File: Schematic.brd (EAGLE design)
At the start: 84 x 96 mm, 64 parts

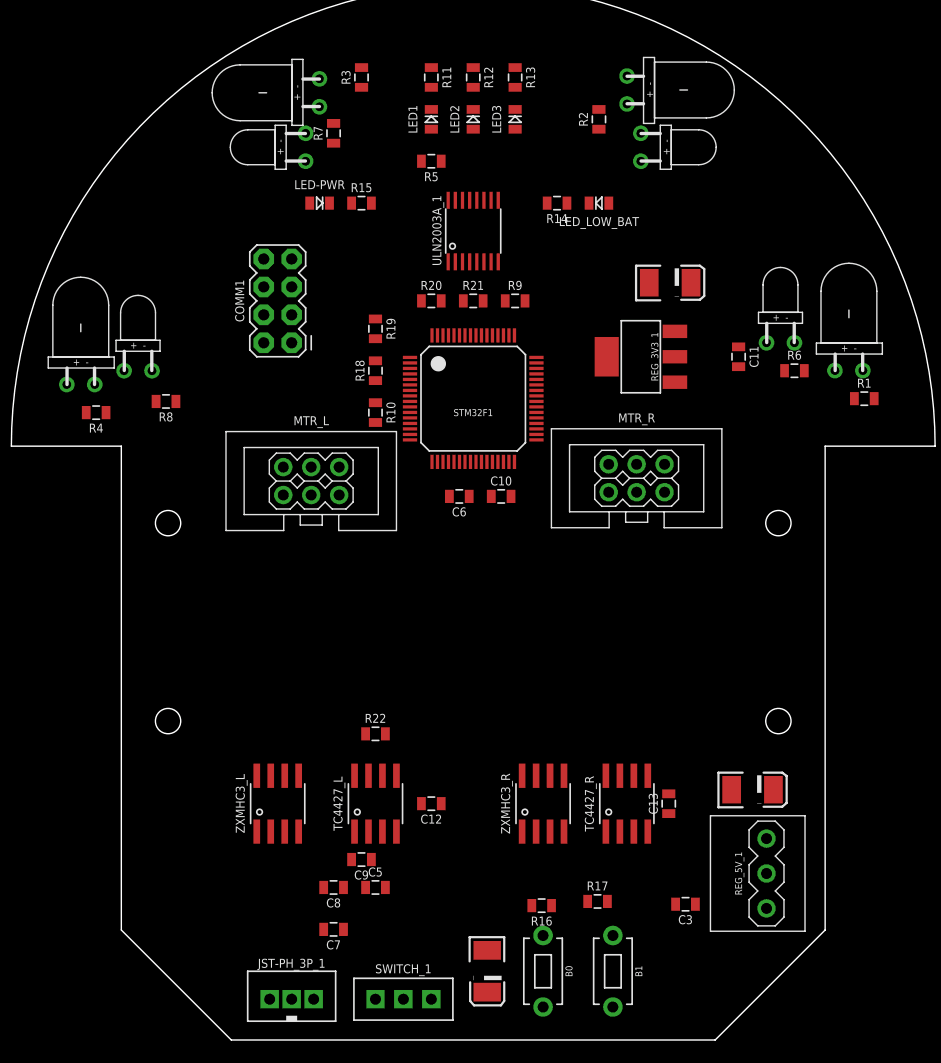
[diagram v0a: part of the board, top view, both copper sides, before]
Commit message: Autoroute only
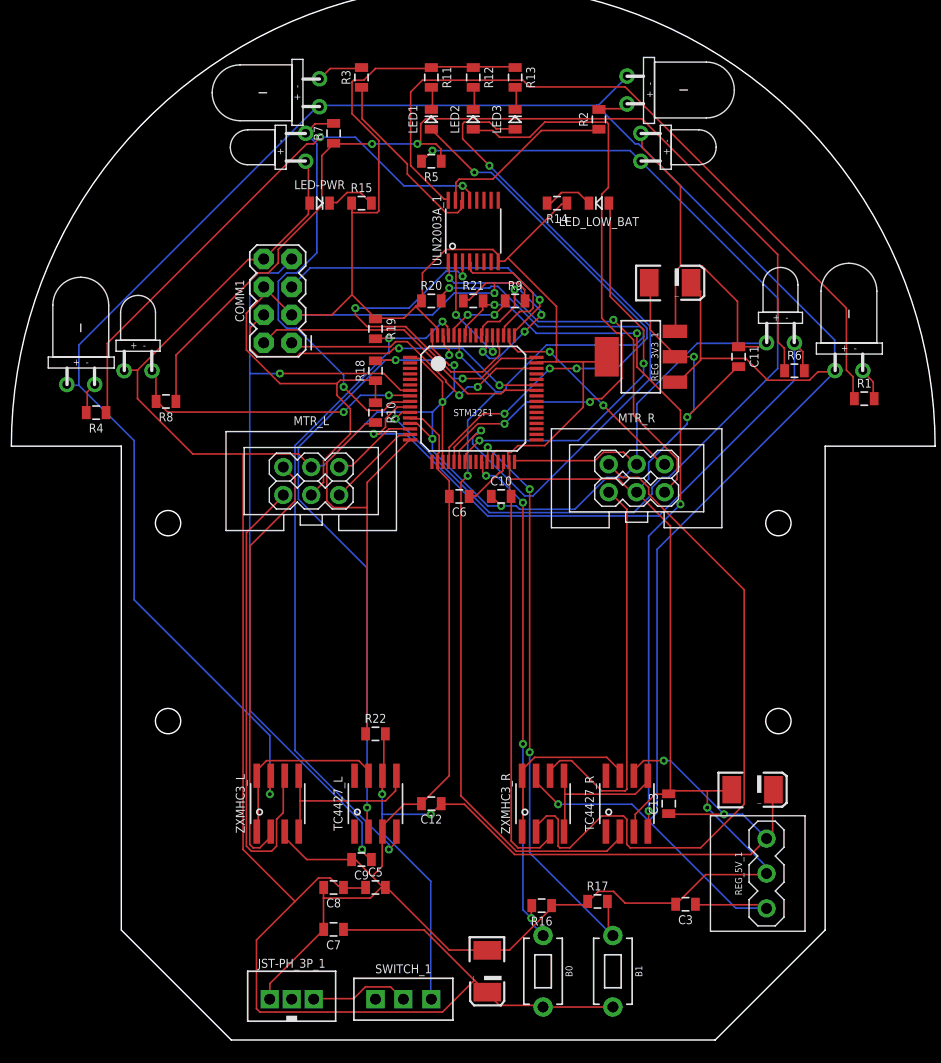
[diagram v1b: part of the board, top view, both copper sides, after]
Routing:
- net GND: track 0.00 -> 425.7 mm, vias 0 -> 4
- net +3V3: track 0.00 -> 295.1 mm, vias 0 -> 5
- net +5V: track 0.00 -> 249.3 mm, vias 0 -> 2
- net RPWM_A: track 0.00 -> 99.3 mm, vias 0 -> 3
- net N$14: track 0.00 -> 91.4 mm, vias 0 -> 2
- net RE_LF: track 0.00 -> 90.4 mm, vias 0 -> 2
- net V+: track 0.00 -> 89.9 mm, vias 0 -> 4
- net NRST: track 0.00 -> 77.1 mm, vias 0 -> 2
- net N$1: track 0.00 -> 68.7 mm
- net RPWM_B: track 0.00 -> 67.5 mm, vias 0 -> 4
- net RMTR+: track 0.00 -> 64.7 mm
- net LPWM_B: track 0.00 -> 63.7 mm, vias 0 -> 3
- net LED3: track 0.00 -> 63.3 mm, vias 0 -> 2
- net LPWM_A: track 0.00 -> 58.7 mm, vias 0 -> 3
- net RE_LD: track 0.00 -> 57.6 mm, vias 0 -> 1
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
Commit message: 013120meeting
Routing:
- net GND: track 425.7 -> 4.02 mm, vias 4 -> 0
- net +3V3: track 295.1 -> 242.1 mm, vias 5 -> 3
- net RPWM_A: track 99.3 -> 57.8 mm, vias 3 -> 2
- net RE_LF: track 90.4 -> 49.1 mm, vias 2 -> 4
- net RMTR+: track 64.7 -> 36.2 mm
- net LED3: track 63.3 -> 36.2 mm
- net LED2: track 56.7 -> 80.9 mm
- net +5V: track 249.3 -> 225.9 mm
- net EM_RD: track 31.0 -> 8.01 mm
- net EM_LD: track 11.1 -> 33.4 mm, vias 2 -> 6
- net N$1: track 68.7 -> 46.5 mm, vias 0 -> 2
- net V+: track 89.9 -> 70.5 mm, vias 4 -> 3
- net LMTR-: track 43.2 -> 25.6 mm
- net LED1: track 51.5 -> 34.1 mm, vias 4 -> 2
- net RE_LD: track 57.6 -> 40.5 mm
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- added copper zone on layer 1, net GND
- added copper zone on layer 16, net GND

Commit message: handroute
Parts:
- removed U$1: (no value), MOUSE_OUTLINE_2WHEEL:MOUSE_OUTLINE_2WHEEL
- added U$2: (no value), MOUSE_OUTLINE_2WHEEL:MOUSE_OUTLINE_2WHEEL
- moved SWITCH_1 116.4 mm to (-44.5, 92.7)
- moved C4 114.6 mm to (-35.6, 94.0), turned to 0 degrees
- moved LED3 113.5 mm to (-73.7, 92.7), turned to 0 degrees
- moved C1 108.8 mm to (-20.3, 94.0)
- moved B1 108.5 mm to (-55.2, 37.5), turned to 0 degrees
- moved LED2 105.9 mm to (-69.8, 92.7), turned to 0 degrees
- moved B0 104.2 mm to (-54.6, 44.5), turned to 0 degrees
- moved LED_LOW_BAT 101.9 mm to (-53.3, 92.7), turned to 0 degrees
- moved LED1 98.3 mm to (-66.0, 92.7), turned to 0 degrees
- moved R17 98.0 mm to (15.2, 104.1)
- moved C3 96.3 mm to (80.0, 104.1), turned to 0 degrees
- moved R16 95.8 mm to (19.1, 104.1), turned to 0 degrees
- moved JST-PH_3P_1 95.6 mm to (-12.7, 92.7)
- moved R1 90.3 mm to (-18.4, 45.1), turned to 180 degrees
- moved EM_1 89.6 mm to (-19.1, 48.3)
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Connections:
- removed net N$14: R5.1, R6.1, R7.1, R8.1
- net GND: now also R5.1, R6.1, R7.1, R8.1
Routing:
- net +3V3: track 242.1 -> 143.8 mm, vias 3 -> 0
- net N$14: track 91.5 -> 0.00 mm, vias 3 -> 0
- net LED2: track 80.9 -> 0.00 mm, vias 2 -> 0
- net NRST: track 71.6 -> 2.72 mm, vias 2 -> 0
- net B1: track 62.0 -> 0.00 mm, vias 2 -> 0
- net RPWM_B: track 60.4 -> 3.54 mm, vias 2 -> 0
- net RPWM_A: track 57.8 -> 3.54 mm, vias 2 -> 0
- net LPWM_B: track 55.6 -> 4.18 mm, vias 4 -> 0
- net LPWM_A: track 54.0 -> 4.18 mm, vias 2 -> 0
- net B0: track 47.6 -> 0.00 mm
- net RE_LF: track 49.1 -> 2.74 mm, vias 4 -> 0
- net RE_LD: track 40.5 -> 2.25 mm, vias 1 -> 0
- net LED3: track 36.2 -> 0.00 mm, vias 2 -> 0
- net RX: track 35.6 -> 0.00 mm, vias 1 -> 0
- net VOLTMETER: track 35.5 -> 0.00 mm, vias 2 -> 0
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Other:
- outline, holes or cut-outs redrawn

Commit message: Routing
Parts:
- moved SWITCH_1 122.9 mm to (22.9, -10.2)
- moved LED3 117.9 mm to (18.4, 19.1)
- moved LED2 112.5 mm to (15.2, 19.1)
- moved JST-PH_3P_1 112.3 mm to (32.4, -10.2)
- moved C1 108.3 mm to (23.5, -5.08)
- moved C2 107.7 mm to (23.5, -0.64)
- moved LED1 107.4 mm to (12.1, 19.1)
- moved R10 96.2 mm to (5.08, 15.2)
- moved R11 92.6 mm to (12.1, 15.2)
- moved LED_LOW_BAT 91.3 mm to (15.2, 32.4), turned to 270 degrees
- moved R12 90.9 mm to (15.2, 15.2)
- moved R13 89.7 mm to (18.4, 15.2)
- moved R22 89.7 mm to (8.26, 15.2)
- moved LED-PWR 89.1 mm to (29.8, 56.5)
- moved C3 82.1 mm to (21.8, 46.2), turned to 180 degrees
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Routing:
- net LPWM_B: track 4.18 -> 63.3 mm
- net LPWM_A: track 4.18 -> 62.5 mm
- net +3V3: track 143.8 -> 187.2 mm
- net VOLTMETER: track 0.00 -> 24.5 mm
- net NRST: track 2.72 -> 27.0 mm, vias 0 -> 1
- net RX: track 0.00 -> 23.0 mm, vias 0 -> 1
- net TX: track 0.00 -> 21.7 mm, vias 0 -> 1
- net SWCLK: track 0.00 -> 19.2 mm, vias 0 -> 1
- net SWDIO: track 0.00 -> 18.6 mm, vias 0 -> 1
- net LED3: track 0.00 -> 18.5 mm
- net LED2: track 0.00 -> 17.5 mm
- net LED1: track 0.00 -> 17.2 mm
- net V+: track 62.8 -> 78.5 mm, vias 0 -> 1
- net B0: track 0.00 -> 14.1 mm
- net N$9: track 0.00 -> 13.9 mm
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
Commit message: Finished routing
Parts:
- moved REG_3V3_1 4.45 mm to (25.4, 56.5)
- moved C4 3.81 mm to (31.8, 55.2)
- moved LED-PWR 3.17 mm to (29.8, 59.7)
- moved R15 3.17 mm to (33.0, 59.7)
- moved C10 2.54 mm to (3.81, 39.4)
- moved C3 0.90 mm to (21.2, 46.9)
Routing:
- net RPWM_A: track 3.54 -> 59.2 mm, vias 0 -> 4
- net RPWM_B: track 3.54 -> 56.5 mm, vias 0 -> 4
- net +3V3: track 187.2 -> 229.3 mm, vias 0 -> 2
- net RE_LF: track 2.74 -> 43.2 mm, vias 0 -> 3
- net RE_RD: track 2.65 -> 42.1 mm, vias 0 -> 2
- net RE_RF: track 2.26 -> 37.7 mm, vias 0 -> 3
- net RE_LD: track 2.25 -> 27.3 mm, vias 0 -> 2
- net SWDIO: track 18.6 -> 22.1 mm
- net RX: track 23.0 -> 25.4 mm
- net TX: track 21.7 -> 23.6 mm
- net +5V: track 250.0 -> 251.7 mm
- net V+: track 78.5 -> 77.0 mm
- net LED3: track 18.5 -> 20.0 mm
- net RMTR-: track 37.4 -> 36.3 mm
- net LPWM_A: track 62.5 -> 61.4 mm
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
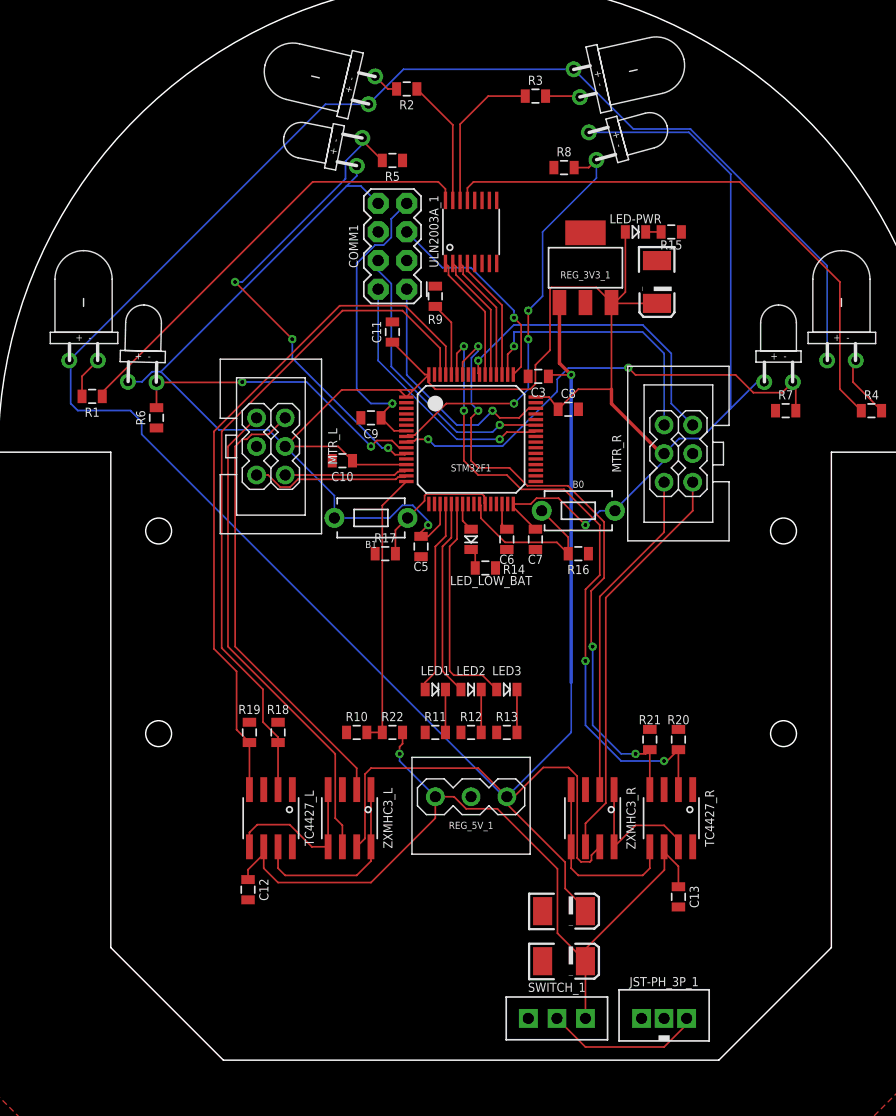
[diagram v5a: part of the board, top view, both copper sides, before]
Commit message: changes trace width
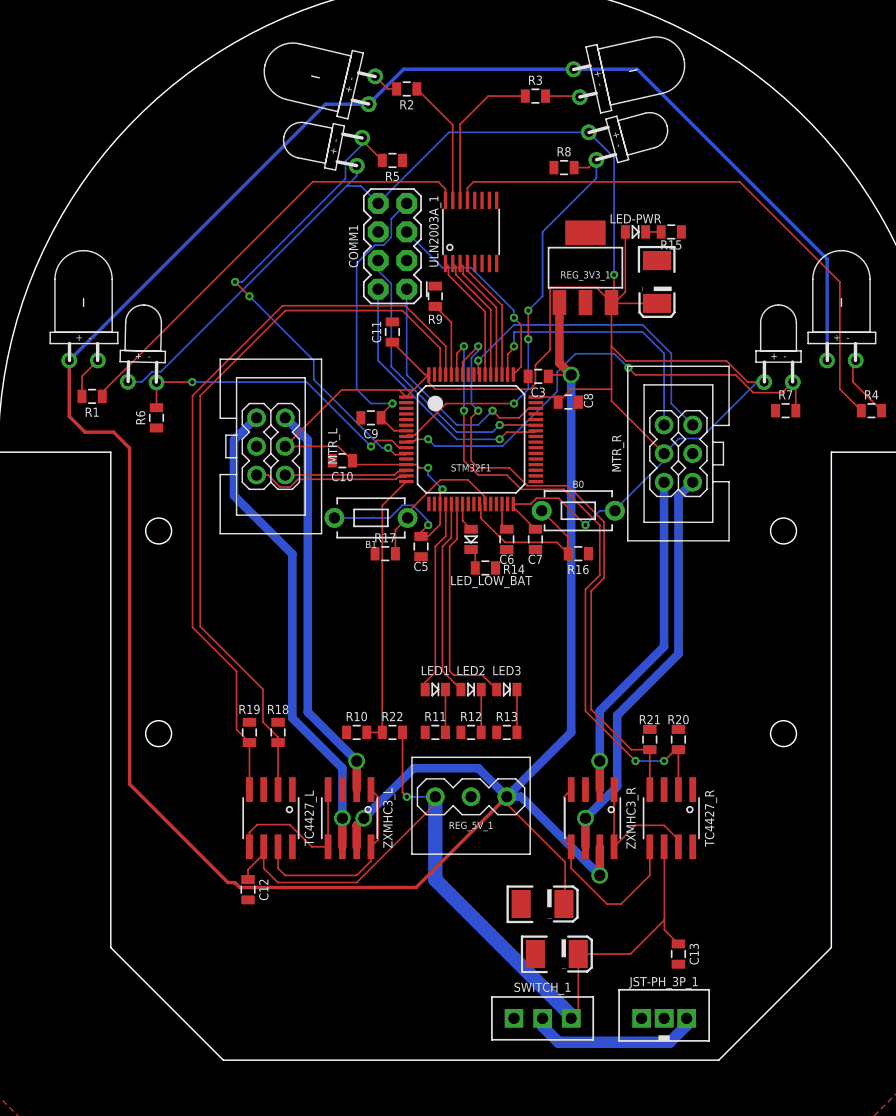
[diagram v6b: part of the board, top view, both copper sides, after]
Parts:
- moved C13 5.08 mm to (33.7, -4.45)
- moved C2 2.01 mm to (21.6, 0.00)
- moved SWITCH_1 1.27 mm to (21.6, -10.2)
- moved C1 0.90 mm to (22.9, -4.45)
- moved C8 0.63 mm to (23.9, 44.6)
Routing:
- net +5V: track 251.7 -> 268.6 mm, vias 1 -> 3
- net V+: track 77.0 -> 81.8 mm
- net LMTR+: track 40.4 -> 35.7 mm, vias 0 -> 1
- net LPWM_B: track 62.3 -> 66.9 mm
- net LPWM_A: track 61.4 -> 66.0 mm
- net N$20: track 16.4 -> 19.4 mm
- net RE_RD: track 42.1 -> 43.5 mm
- net N$9: track 13.9 -> 15.3 mm
- net B1: track 12.4 -> 13.4 mm
- net RPWM_B: track 56.5 -> 55.4 mm, vias 4 -> 2
- net RPWM_A: track 59.2 -> 58.5 mm
- net N$18: track 17.3 -> 17.8 mm
- net +3V3: track 229.3 -> 229.8 mm, vias 2 -> 5
- net LMTR-: track 43.4 -> 42.9 mm, vias 0 -> 1
- net RMTR-: vias 0 -> 1
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
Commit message: Routing
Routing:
- net +3V3: track 229.8 -> 234.2 mm
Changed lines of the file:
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@@
 <wire x1="32.385" y1="40.005" x2="33.7227375" y2="41.3427375" width="0.1524" layer="16"/>
 <wire x1="33.7227375" y1="41.3427375" x2="35.6277375" y2="41.3427375" width="0.1524" layer="16"/>
-<wire x1="38.3032" y1="44.0182" x2="38.1" y2="43.815" width="0.1524" layer="16"/>
-<wire x1="38.1" y1="43.815" x2="35.6277375" y2="41.3427375" width="0.1524" layer="16"/>
 <wire x1="-13.983928125" y1="46.3838125" x2="-15.239671875" y2="46.3838125" width="0.1524" layer="16"/>
 <wire x1="-13.0931625" y1="47.274578125" x2="-13.983928125" y2="46.3838125" width="0.1524" layer="16"/>
@@
 <wire x1="8.01946875" y1="34.29" x2="9.13706875" y2="35.4076" width="0.1524" layer="16"/>
 <wire x1="12.49" y1="33.71" x2="11.43" y2="32.65" width="0.1524" layer="1"/>
-<wire x1="31.75" y1="53.345" x2="27.94" y2="53.345" width="0.1524" layer="1"/>
-<wire x1="27.94" y1="53.345" x2="27.782" y2="53.345" width="0.1524" layer="1"/>
-<wire x1="27.782" y1="53.345" x2="27.711" y2="53.416" width="0.1524" layer="1"/>
-<wire x1="28.945" y1="54.35" x2="27.94" y2="53.345" width="0.1524" layer="1"/>
-<wire x1="28.945" y1="59.69" x2="28.945" y2="54.35" width="0.1524" layer="1"/>
-<wire x1="27.711" y1="53.274" x2="27.711" y2="49.53" width="0.1524" layer="1"/>
-<wire x1="27.711" y1="49.53" x2="27.711" y2="45.72" width="0.1524" layer="1"/>
-<wire x1="27.711" y1="53.274" x2="27.782" y2="53.345" width="0.1524" layer="1"/>
-<wire x1="22.2509" y1="54.6281875" x2="22.3848125" y2="54.7621" width="0.1524" layer="1"/>
-<wire x1="26.3649" y1="54.7621" x2="27.546" y2="53.581" width="0.1524" layer="1"/>
-<wire x1="27.546" y1="53.581" x2="27.711" y2="53.416" width="0.1524" layer="1"/>
-<wire x1="22.3848125" y1="54.7621" x2="26.3649" y2="54.7621" width="0.1524" layer="1"/>
-<wire x1="22.2509" y1="54.6281875" x2="22.2509" y2="49.1749" width="0.1524" layer="1"/>
+<wire x1="28.945" y1="54.35" x2="28.945" y2="59.69" width="0.1524" layer="1"/>
+<wire x1="27.711" y1="45.72" x2="27.711" y2="49.53" width="0.1524" layer="1"/>
+<wire x1="22.2509" y1="49.1749" x2="22.2509" y2="54.6281875" width="0.1524" layer="1"/>
 <wire x1="20.4892875" y1="45.72" x2="20.955" y2="46.1857125" width="0.1524" layer="1"/>
 <wire x1="12.065" y1="45.72" x2="11.4425" y2="46.3425" width="0.1524" layer="1"/>
@@
 <wire x1="27.94" y1="66.294865625" x2="27.94" y2="55.88" width="0.1524" layer="16"/>
 <via x="27.94" y="55.88" extent="1-16" drill="0.35"/>
-<wire x1="27.94" y1="55.88" x2="27.94" y2="53.975" width="0.1524" layer="1"/>
-<wire x1="27.94" y1="53.975" x2="27.546" y2="53.581" width="0.1524" layer="1"/>
 <wire x1="6.985" y1="62.23" x2="13.2899875" y2="68.5349875" width="0.1524" layer="16"/>
 <wire x1="13.2899875" y1="68.5349875" x2="25.699878125" y2="68.5349875" width="0.1524" layer="16"/>
@@
 <wire x1="10.668" y1="38.735" x2="10.378" y2="39.025" width="0.1524" layer="1"/>
 <wire x1="39.80105625" y1="46.355" x2="41.275" y2="46.355" width="0.1524" layer="1"/>
-<wire x1="38.3032" y1="44.0182" x2="40.64" y2="46.355" width="0.1524" layer="16"/>
+<wire x1="35.6277375" y1="41.3427375" x2="40.64" y2="46.355" width="0.1524" layer="16"/>
 <wire x1="40.64" y1="46.355" x2="41.275" y2="46.355" width="0.1524" layer="16"/>
+<wire x1="22.2509" y1="54.6281875" x2="22.8677125" y2="55.245" width="0.1524" layer="1"/>
+<wire x1="22.8677125" y1="55.245" x2="23.495" y2="55.245" width="0.1524" layer="1"/>
+<wire x1="23.495" y1="55.245" x2="24.13" y2="54.61" width="0.1524" layer="1"/>
+<wire x1="24.13" y1="52.07" x2="24.765" y2="51.435" width="0.1524" layer="1"/>
+<wire x1="26.67" y1="51.435" x2="24.765" y2="51.435" width="0.1524" layer="1"/>
+<wire x1="24.13" y1="54.61" x2="24.13" y2="52.07" width="0.1524" layer="1"/>
+<wire x1="27.711" y1="53.416" x2="27.711" y2="52.476" width="0.1524" layer="1"/>
+<wire x1="27.711" y1="52.476" x2="26.67" y2="51.435" width="0.1524" layer="1"/>
+<wire x1="27.711" y1="53.416" x2="28.645" y2="54.35" width="0.1524" layer="1"/>
+<wire x1="28.645" y1="54.35" x2="28.945" y2="54.35" width="0.1524" layer="1"/>
+<wire x1="27.711" y1="53.416" x2="31.679" y2="53.416" width="0.1524" layer="1"/>
+<wire x1="31.679" y1="53.416" x2="31.75" y2="53.345" width="0.1524" layer="1"/>
+<wire x1="27.94" y1="55.88" x2="27.94" y2="53.645" width="0.1524" layer="1"/>
+<wire x1="27.94" y1="53.645" x2="27.711" y2="53.416" width="0.1524" layer="1"/>
+<wire x1="27.711" y1="49.53" x2="27.711" y2="53.416" width="0.1524" layer="1"/>
 </signal>
 <signal name="TX">
@@
 <via x="20.32" y="50.165" extent="1-16" drill="0.35"/>
 <wire x1="26.37011875" y1="66.085009375" x2="26.37011875" y2="64.47011875" width="0.1524" layer="16"/>
-<wire x1="26.37011875" y1="64.47011875" x2="21.59" y2="59.69" width="0.1524" layer="16"/>
-<wire x1="21.59" y1="59.69" x2="21.59" y2="53.975" width="0.1524" layer="16"/>
-<wire x1="21.59" y1="53.975" x2="20.32" y2="52.705" width="0.1524" layer="16"/>
+<wire x1="26.37011875" y1="64.47011875" x2="20.32" y2="58.42" width="0.1524" layer="16"/>
+<wire x1="20.32" y1="58.42" x2="20.32" y2="52.705" width="0.1524" layer="16"/>
 <via x="20.32" y="52.705" extent="1-16" drill="0.35"/>
 <wire x1="20.32" y1="52.705" x2="20.32" y2="50.165" width="0.1524" layer="1"/>

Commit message: finished routing
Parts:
- moved B0 51.1 mm to (0.64, -10.2), turned to 180 degrees
- moved B1 44.7 mm to (10.8, -10.2)
- moved R16 41.5 mm to (5.71, -5.71), turned to 270 degrees
- moved R17 37.0 mm to (10.8, -5.71), turned to 270 degrees
- moved C3 13.5 mm to (25.7, 59.6)
- moved COMM1 10.3 mm to (-1.91, 56.5)
- moved C8 9.49 mm to (21.8, 53.8), turned to 180 degrees
- moved C5 7.62 mm to (10.8, 39.4)
- moved ULN2003A_1 7.00 mm to (15.6, 66.7)
- moved R15 6.84 mm to (39.4, 62.2)
- moved C9 6.35 mm to (6.35, 49.5)
- moved LED_LOW_BAT 6.35 mm to (15.2, 38.7)
- moved STM32F1 6.35 mm to (15.2, 47.6)
- moved C11 6.02 mm to (10.2, 56.5)
- moved C10 5.75 mm to (3.17, 45.1)
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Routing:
- net GND: track 0.00 -> 112.1 mm
- net B1: track 13.4 -> 85.7 mm
- net +5V: track 268.6 -> 197.4 mm, vias 3 -> 1
- net B0: track 15.2 -> 80.4 mm
- net +3V3: track 234.2 -> 277.1 mm, vias 5 -> 3
- net TX: track 23.6 -> 50.8 mm
- net SWDIO: track 22.1 -> 41.5 mm
- net RE_LF: track 43.2 -> 25.2 mm, vias 3 -> 2
- net RX: track 25.4 -> 43.0 mm
- net LPWM_A: track 66.0 -> 54.4 mm, vias 0 -> 2
- net LPWM_B: track 66.9 -> 56.4 mm, vias 0 -> 2
- net LED2: track 17.5 -> 27.3 mm, vias 0 -> 2
- net LED1: track 17.2 -> 26.7 mm, vias 0 -> 2
- net NRST: track 27.0 -> 18.2 mm, vias 1 -> 0
- net LED3: track 20.0 -> 28.3 mm, vias 0 -> 2
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- removed copper zone on layer 1, net GND
